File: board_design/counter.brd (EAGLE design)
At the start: 54.3 x 94 mm, 24 parts, among them IC1 7805T

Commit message: Board update
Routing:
- net CLR: track 86.2 -> 89.8 mm
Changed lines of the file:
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@@
 <wire x1="54.28" y1="93.98" x2="0" y2="93.98" width="0" layer="20"/>
 <hole x="50.8" y="91.44" drill="3.81"/>
-<hole x="17.78" y="58.42" drill="3.81"/>
+<hole x="19.05" y="58.42" drill="7.62"/>
 <hole x="2.54" y="2.54" drill="3.81"/>
 <hole x="50.8" y="2.54" drill="3.81"/>
@@
 <wire x1="44.45" y1="27.94" x2="46.99" y2="27.94" width="0.6096" layer="25"/>
 <wire x1="7.62" y1="74.93" x2="10.16" y2="74.93" width="0.6096" layer="25"/>
-<wire x1="7.62" y1="72.39" x2="8.89" y2="72.39" width="0.6096" layer="26"/>
-<wire x1="8.89" y1="73.66" x2="8.89" y2="72.39" width="0.6096" layer="25"/>
-<wire x1="10.16" y1="72.39" x2="8.89" y2="72.39" width="0.6096" layer="26"/>
-<wire x1="8.89" y1="72.39" x2="8.89" y2="71.12" width="0.6096" layer="25"/>
+<wire x1="10.16" y1="72.39" x2="7.62" y2="72.39" width="0.6096" layer="26"/>
+<wire x1="8.89" y1="73.66" x2="8.89" y2="71.12" width="0.6096" layer="25"/>
 <wire x1="12.7" y1="85.09" x2="12.7" y2="82.55" width="0.6096" layer="26"/>
-<wire x1="13.97" y1="83.82" x2="15.24" y2="83.82" width="0.6096" layer="26"/>
-<wire x1="16.51" y1="83.82" x2="15.24" y2="83.82" width="0.6096" layer="26"/>
-<wire x1="15.24" y1="85.09" x2="15.24" y2="83.82" width="0.6096" layer="25"/>
-<wire x1="15.24" y1="83.82" x2="15.24" y2="82.55" width="0.6096" layer="25"/>
+<wire x1="16.51" y1="83.82" x2="13.97" y2="83.82" width="0.6096" layer="26"/>
+<wire x1="15.24" y1="85.09" x2="15.24" y2="82.55" width="0.6096" layer="25"/>
 </plain>
 <attributes>
@@
 <wire x1="39.37" y1="87.63" x2="39.37" y2="81.28" width="0.6096" layer="16"/>
 <wire x1="39.37" y1="81.28" x2="30.48" y2="72.39" width="0.6096" layer="16"/>
-<wire x1="30.48" y1="72.39" x2="15.24" y2="72.39" width="0.6096" layer="16"/>
-<wire x1="15.24" y1="72.39" x2="13.97" y2="71.12" width="0.6096" layer="16"/>
-<wire x1="13.97" y1="55.88" x2="22.86" y2="46.99" width="0.6096" layer="16"/>
-<wire x1="13.97" y1="71.12" x2="13.97" y2="55.88" width="0.6096" layer="16"/>
+<wire x1="30.48" y1="72.39" x2="12.7" y2="72.39" width="0.6096" layer="16"/>
+<wire x1="12.7" y1="72.39" x2="11.43" y2="71.12" width="0.6096" layer="16"/>
+<wire x1="11.43" y1="58.42" x2="22.86" y2="46.99" width="0.6096" layer="16"/>
+<wire x1="11.43" y1="71.12" x2="11.43" y2="58.42" width="0.6096" layer="16"/>
 <wire x1="22.86" y1="46.99" x2="22.86" y2="44.45" width="0.6096" layer="16"/>
 </signal>

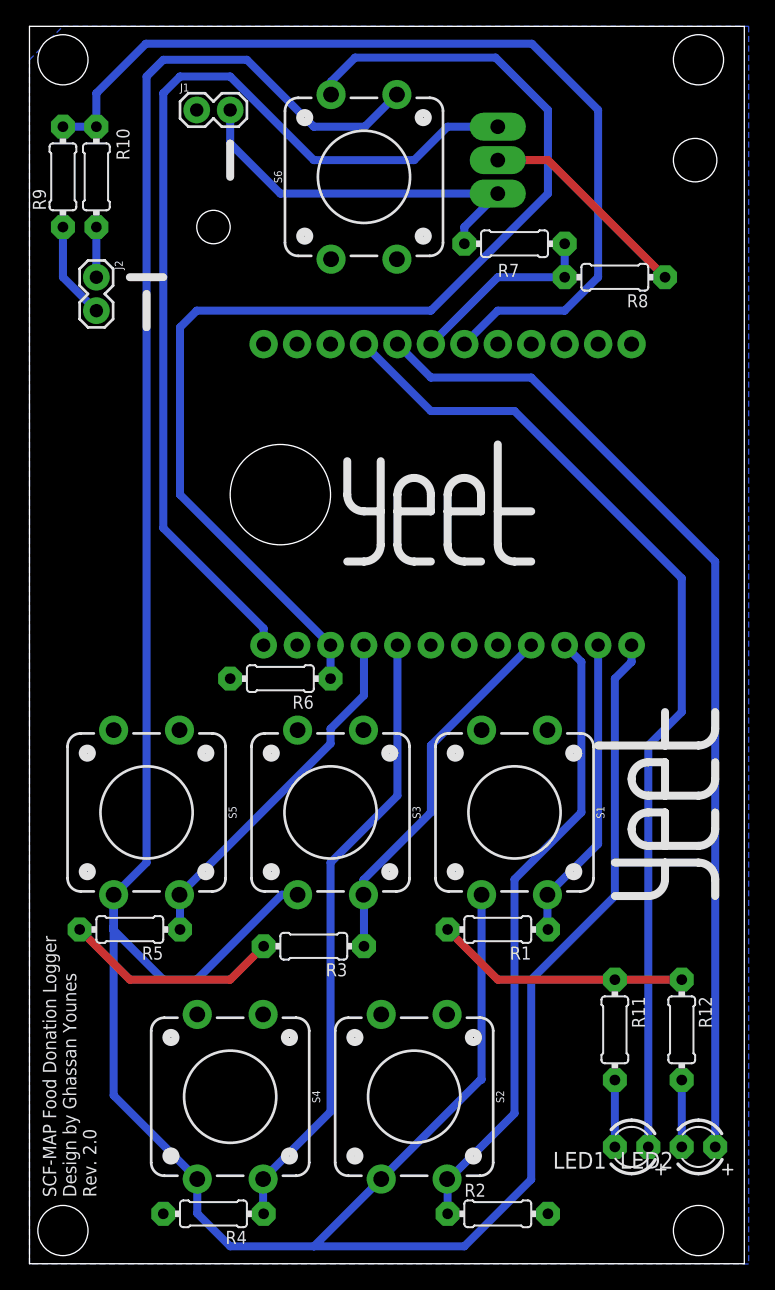
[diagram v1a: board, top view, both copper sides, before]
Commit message: Implemented sleep and wakeup
Only misc and prep meals actually wake it up
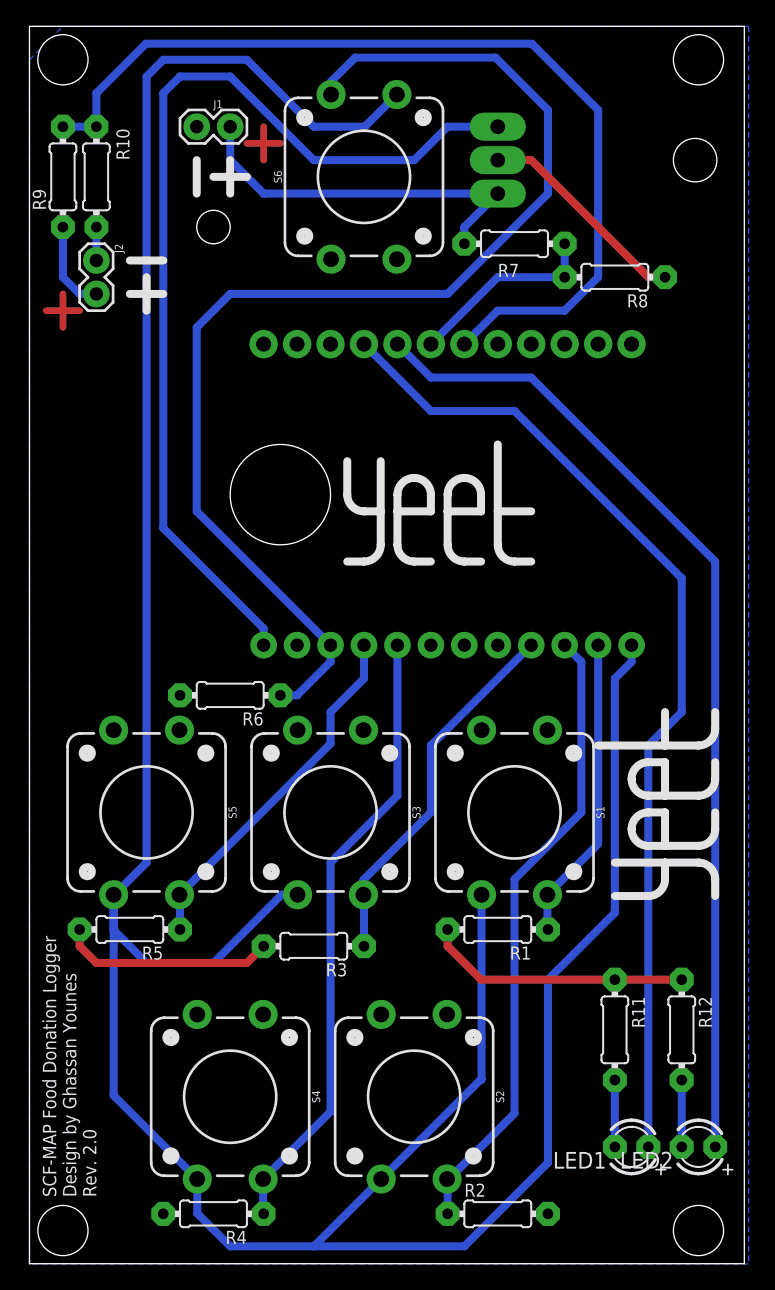
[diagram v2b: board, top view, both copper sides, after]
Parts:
- moved R6 4.02 mm to (15.2, 43.2)
- moved J1 1.27 mm to (12.7, 86.4)
- moved J2 1.27 mm to (5.08, 76.2)
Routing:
- net N$2: track 0.00 -> 5.08 mm
- net N$1: track 0.00 -> 5.08 mm
- net CLR: track 89.8 -> 91.6 mm
- net BAT-: track 3.81 -> 2.54 mm
- net VBUS: track 237.8 -> 236.7 mm
- net BAT+: track 7.40 -> 6.88 mm
- net SOLAR+: track 29.3 -> 28.8 mm

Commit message: Modified board not to have ADC on the boot pins (woops)
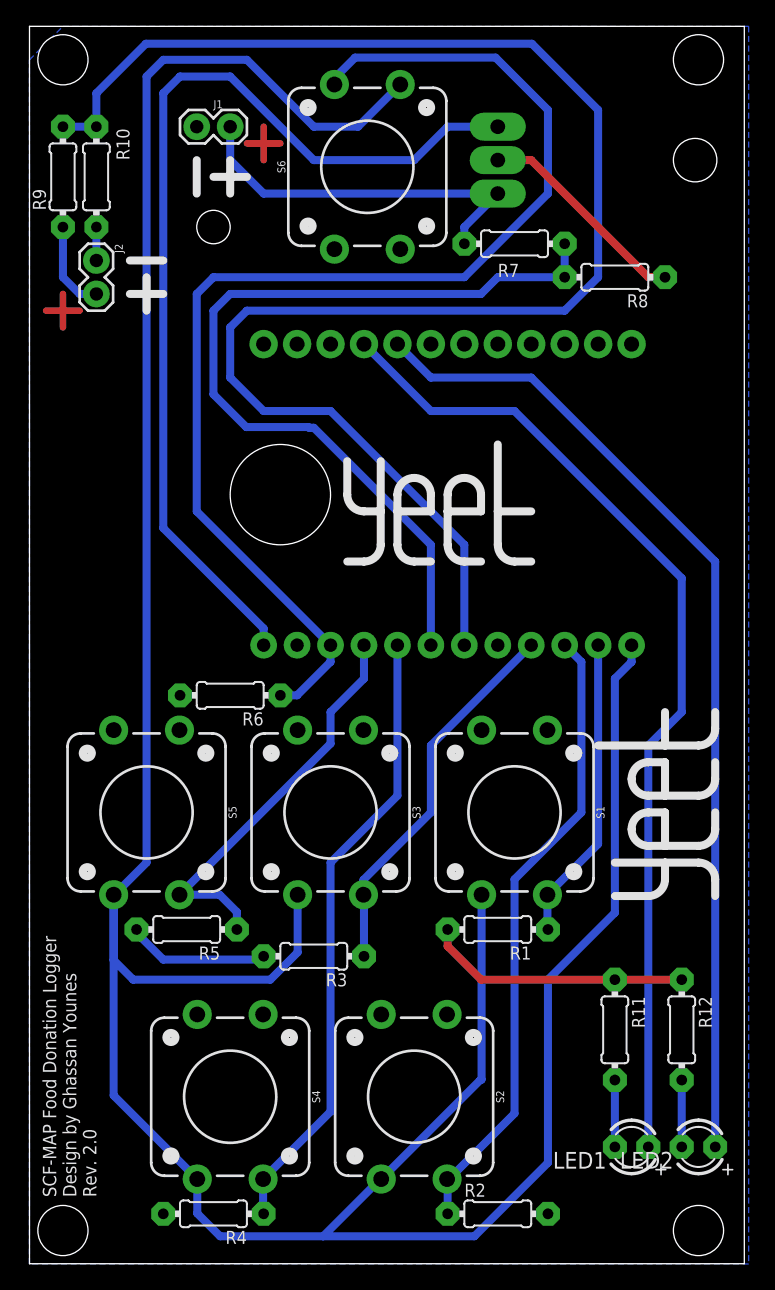
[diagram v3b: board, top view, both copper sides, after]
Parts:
- moved R5 4.32 mm to (11.9, 25.4)
- moved S6 0.80 mm to (25.7, 83.3)
- moved R3 0.76 mm to (21.6, 23.4)
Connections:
- net ADCBAT: now also U$1.32; no longer U$1.2
- net ADCSOL: now also U$1.33; no longer U$1.15
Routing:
- net ADCBAT: track 71.8 -> 123.5 mm
- net ADCSOL: track 14.8 -> 65.5 mm
- net GND: track 52.8 -> 47.3 mm
- net VBUS: track 236.7 -> 240.6 mm
- net MISC: track 27.4 -> 31.0 mm
- net FEESH: track 28.2 -> 28.9 mm
- net CLR: track 91.6 -> 92.2 mm

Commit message: couple changes to board
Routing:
- net CLR: track 92.2 -> 95.4 mm
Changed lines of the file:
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@@
 <wire x1="23.154" y1="89.562" x2="23.154" y2="90.037225" width="0.6096" layer="16"/>
 <wire x1="23.154" y1="90.037225" x2="24.723475" y2="91.6067" width="0.6096" layer="16"/>
-<wire x1="24.723475" y1="91.6067" x2="35.3933" y2="91.6067" width="0.6096" layer="16"/>
-<wire x1="35.3933" y1="91.6067" x2="39.37" y2="87.63" width="0.6096" layer="16"/>
-<wire x1="39.37" y1="87.63" x2="39.37" y2="81.28" width="0.6096" layer="16"/>
-<wire x1="39.37" y1="81.28" x2="33.02" y2="74.93" width="0.6096" layer="16"/>
-<wire x1="33.02" y1="74.93" x2="13.97" y2="74.93" width="0.6096" layer="16"/>
+<wire x1="24.723475" y1="91.6067" x2="36.9173" y2="91.6067" width="0.6096" layer="16"/>
+<wire x1="36.9173" y1="91.6067" x2="40.894" y2="87.63" width="0.6096" layer="16"/>
+<wire x1="40.894" y1="87.63" x2="40.894" y2="81.026" width="0.6096" layer="16"/>
+<wire x1="40.894" y1="81.026" x2="34.798" y2="74.93" width="0.6096" layer="16"/>
+<wire x1="34.798" y1="74.93" x2="13.97" y2="74.93" width="0.6096" layer="16"/>
 <wire x1="13.97" y1="74.93" x2="12.7" y2="73.66" width="0.6096" layer="16"/>
 <wire x1="12.7" y1="57.15" x2="22.86" y2="46.99" width="0.6096" layer="16"/>
@@
 <contactref element="R8" pad="2"/>
 <wire x1="40.64" y1="77.47" x2="40.64" y2="74.93" width="0.6096" layer="16"/>
-<wire x1="40.64" y1="74.93" x2="35.56" y2="74.93" width="0.6096" layer="16"/>
+<wire x1="40.64" y1="74.93" x2="39.37" y2="73.66" width="0.6096" layer="16"/>
 <contactref element="U$1" pad="33"/>
-<wire x1="35.56" y1="74.93" x2="34.29" y2="73.66" width="0.6096" layer="16"/>
-<wire x1="34.29" y1="73.66" x2="15.24" y2="73.66" width="0.6096" layer="16"/>
+<wire x1="39.37" y1="73.66" x2="15.24" y2="73.66" width="0.6096" layer="16"/>
 <wire x1="15.24" y1="73.66" x2="13.97" y2="72.39" width="0.6096" layer="16"/>
 <wire x1="13.97" y1="72.39" x2="13.97" y2="66.04" width="0.6096" layer="16"/>
